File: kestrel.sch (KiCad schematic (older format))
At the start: 9 parts, among them J1 171971-0003, J2 171971-0003, J3 171971-0005, J4 171971-0005, J6 171971-0003, J7 Conn_02x02_Odd_Even

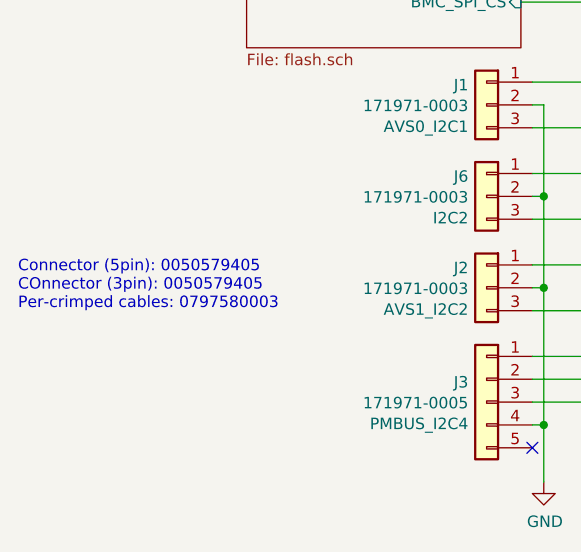
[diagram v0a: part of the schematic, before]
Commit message: versa-adapter: Fix 3pin connector part number.
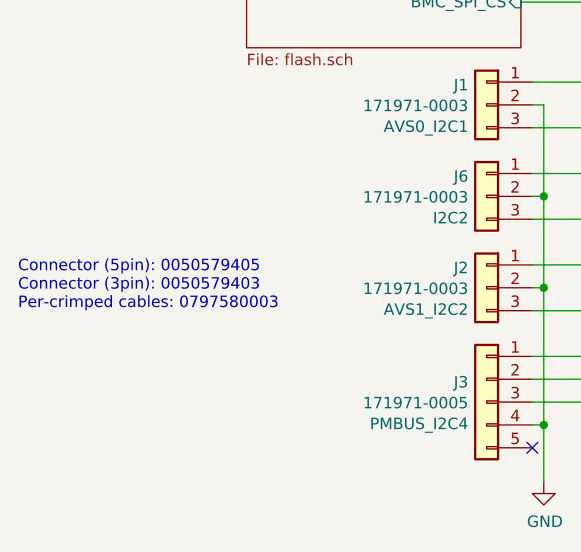
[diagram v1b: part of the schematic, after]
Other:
- note added: "Connector (5pin): 0050579405\nConnector (3pin): 0050579403\nPer-crimped cables: 0797580003\n"
- note removed: "Connector (5pin): 0050579405\nCOnnector (3pin): 0050579405\nPer-crimped cables: 0797580003\n"
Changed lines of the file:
@@
 NoConn ~ 4350 6550
 Text Notes 2100 5950 0    50   ~ 0
-Connector (5pin): 0050579405\nCOnnector (3pin): 0050579405\nPer-crimped cables: 0797580003\n
+Connector (5pin): 0050579405\nConnector (3pin): 0050579403\nPer-crimped cables: 0797580003\n
 $EndSCHEMATC
